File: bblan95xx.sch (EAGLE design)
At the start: 52 parts, among them IC1 LAN9512, IC2 93ST, Q1 25MHz

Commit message: improve pcb yield by optimizing PCB to revision 2
However the pinheaders remain either for castellations but more
because they are in the original schematic. (While the big
vias as holes instead are not)

When creating a panel the pinheaders can be removed.
But beware of the lables not to go away, too...

Signed-off-by: Stephan Baerwolf <stephan@matrixstorm.com>
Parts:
- added Q2: (no value), crystal:CRYSTALHC49S
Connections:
- net XI: now also Q2.2
- net XO: now also Q2.1
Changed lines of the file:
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@@
 <layers>
 <layer number="1" name="Top" color="4" fill="1" visible="no" active="no"/>
+<layer number="2" name="Route2" color="1" fill="3" visible="no" active="no"/>
+<layer number="3" name="Route3" color="4" fill="3" visible="no" active="no"/>
+<layer number="14" name="Route14" color="1" fill="6" visible="no" active="no"/>
+<layer number="15" name="Route15" color="4" fill="6" visible="no" active="no"/>
 <layer number="16" name="Bottom" color="1" fill="1" visible="no" active="no"/>
 <layer number="17" name="Pads" color="2" fill="1" visible="no" active="no"/>
@@
 <part name="R8" library="resistor" deviceset="R-EU_" device="R0402"/>
 <part name="C30" library="resistor" deviceset="C-EU" device="C0603K" value=".1u"/>
+<part name="Q2" library="crystal" deviceset="CRYSTAL" device="HC49S"/>
 </parts>
 <sheets>
@@
 <instance part="R8" gate="G$1" x="-149.86" y="73.66" rot="R180"/>
 <instance part="C30" gate="G$1" x="-205.74" y="93.98" rot="R90"/>
+<instance part="Q2" gate="G$1" x="-185.42" y="-96.52" rot="R90"/>
 </instances>
 <busses>
@@
 <wire x1="-195.58" y1="-88.9" x2="-190.5" y2="-88.9" width="0.1524" layer="91"/>
 <wire x1="-190.5" y1="-91.44" x2="-190.5" y2="-88.9" width="0.1524" layer="91"/>
-<wire x1="-190.5" y1="-88.9" x2="-182.88" y2="-88.9" width="0.1524" layer="91"/>
+<wire x1="-190.5" y1="-88.9" x2="-185.42" y2="-88.9" width="0.1524" layer="91"/>
 <pinref part="Q1" gate="G$1" pin="2"/>
+<wire x1="-185.42" y1="-88.9" x2="-182.88" y2="-88.9" width="0.1524" layer="91"/>
 <wire x1="-195.58" y1="-93.98" x2="-195.58" y2="-88.9" width="0.1524" layer="91"/>
 <junction x="-195.58" y="-88.9"/>
@@
 <pinref part="IC1" gate="G$2" pin="61XI"/>
 <wire x1="-182.88" y1="-93.98" x2="-177.8" y2="-93.98" width="0.1524" layer="91"/>
+<pinref part="Q2" gate="G$1" pin="2"/>
+<wire x1="-185.42" y1="-93.98" x2="-185.42" y2="-88.9" width="0.1524" layer="91"/>
+<junction x="-185.42" y="-88.9"/>
 </segment>
 </net>
@@
 <segment>
 <pinref part="R5" gate="G$1" pin="1"/>
-<wire x1="-182.88" y1="-104.14" x2="-190.5" y2="-104.14" width="0.1524" layer="91"/>
+<wire x1="-182.88" y1="-104.14" x2="-185.42" y2="-104.14" width="0.1524" layer="91"/>
 <pinref part="C23" gate="G$1" pin="2"/>
+<wire x1="-185.42" y1="-104.14" x2="-190.5" y2="-104.14" width="0.1524" layer="91"/>
 <wire x1="-190.5" y1="-101.6" x2="-190.5" y2="-104.14" width="0.1524" layer="91"/>
 <wire x1="-190.5" y1="-104.14" x2="-195.58" y2="-104.14" width="0.1524" layer="91"/>
@@
 <wire x1="-177.8" y1="-99.06" x2="-182.88" y2="-99.06" width="0.1524" layer="91"/>
 <wire x1="-182.88" y1="-99.06" x2="-182.88" y2="-104.14" width="0.1524" layer="91"/>
+<pinref part="Q2" gate="G$1" pin="1"/>
+<wire x1="-185.42" y1="-99.06" x2="-185.42" y2="-104.14" width="0.1524" layer="91"/>
+<junction x="-185.42" y="-104.14"/>
 </segment>
 </net>

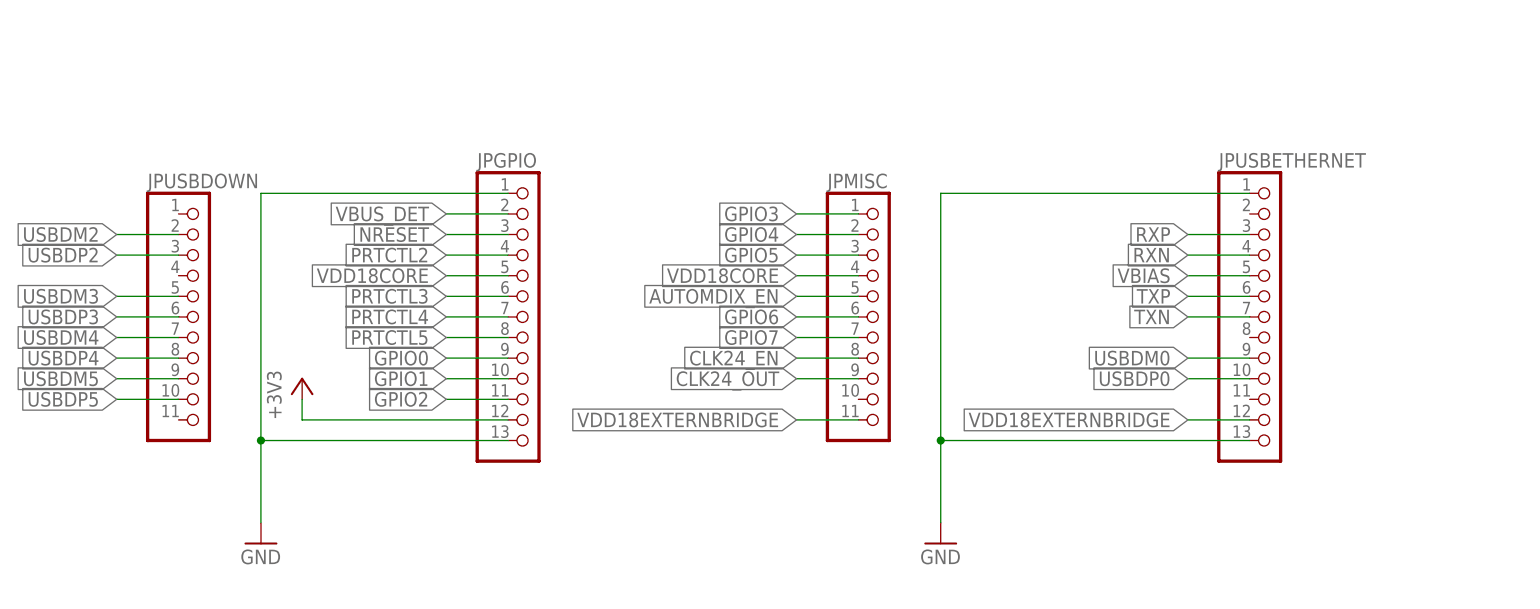
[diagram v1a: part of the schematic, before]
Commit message: mutilate schematic (remove pinheaders)...
...to finalize rev2 panelizeable board.

Signed-off-by: Stephan Baerwolf <stephan@matrixstorm.com>
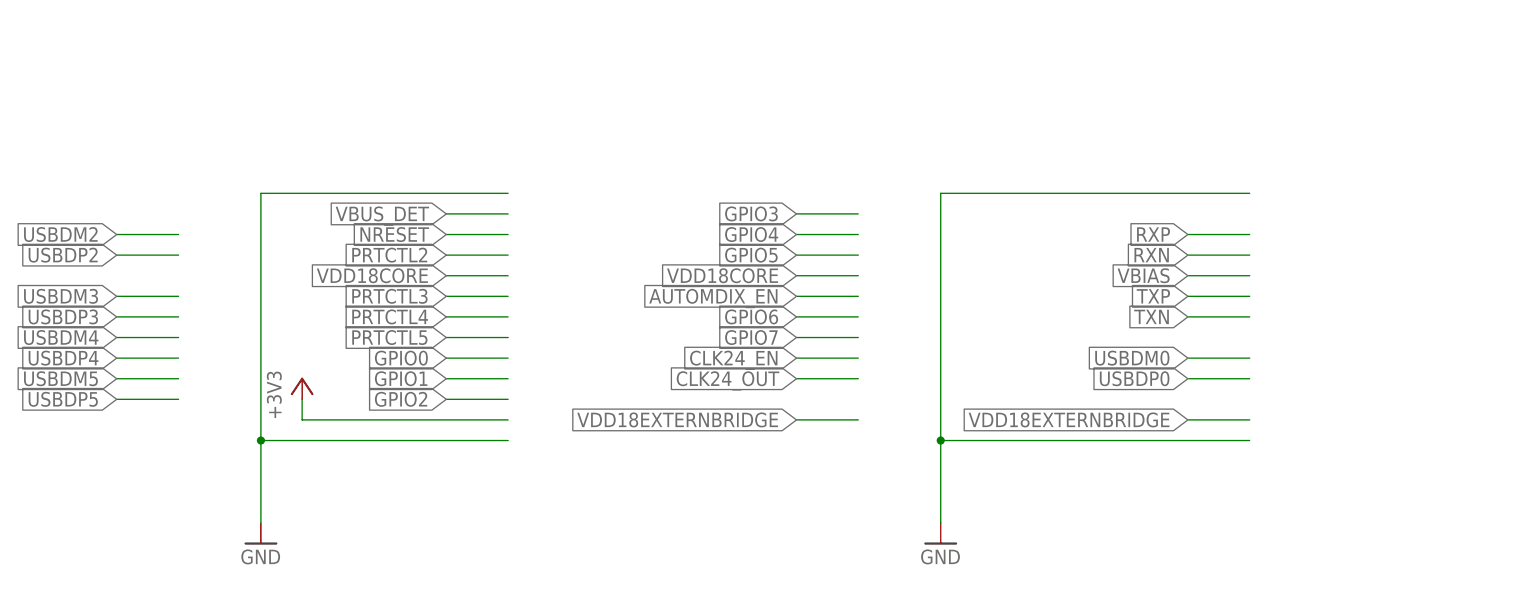
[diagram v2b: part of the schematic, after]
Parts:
- removed JPGPIO, JPUSBETHERNET: (no value), pinhead:PINHD-1X13
- removed JPMISC, JPUSBDOWN: (no value), pinhead:PINHD-1X11
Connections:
- net +3V3: no longer JPGPIO.12
- net AUTOMDIX_EN: no longer JPMISC.5
- net CLK24_EN: no longer JPMISC.8
- net CLK24_OUT: no longer JPMISC.9
- net GND: no longer JPGPIO.1, JPGPIO.13, JPUSBETHERNET.1, JPUSBETHERNET.13
- net GPIO0: no longer JPGPIO.9
- net GPIO1: no longer JPGPIO.10
- net GPIO2: no longer JPGPIO.11
- net GPIO3: no longer JPMISC.1
- net GPIO4: no longer JPMISC.2
- net GPIO5: no longer JPMISC.3
- net GPIO6: no longer JPMISC.6
- net GPIO7: no longer JPMISC.7
- net NRESET: no longer JPGPIO.3
- net PRTCTL2: no longer JPGPIO.4
- net PRTCTL3: no longer JPGPIO.6
- net PRTCTL4: no longer JPGPIO.7
- net PRTCTL5: no longer JPGPIO.8
- net RXN: no longer JPUSBETHERNET.4
- net RXP: no longer JPUSBETHERNET.3
- net TXN: no longer JPUSBETHERNET.7
- net TXP: no longer JPUSBETHERNET.6
- net USBDM0: no longer JPUSBETHERNET.9
- net USBDM2: no longer JPUSBDOWN.2
- net USBDM3: no longer JPUSBDOWN.5
- net USBDM4: no longer JPUSBDOWN.7
- net USBDM5: no longer JPUSBDOWN.9
- net USBDP0: no longer JPUSBETHERNET.10
- net USBDP2: no longer JPUSBDOWN.3
- net USBDP3: no longer JPUSBDOWN.6
- net USBDP4: no longer JPUSBDOWN.8
- net USBDP5: no longer JPUSBDOWN.10
- net VBIAS: no longer JPUSBETHERNET.5
- net VBUS_DET: no longer JPGPIO.2
- net VDD18CORE: no longer JPGPIO.5, JPMISC.4
- net VDD18EXTERNBRIDGE: no longer JPMISC.11, JPUSBETHERNET.12
